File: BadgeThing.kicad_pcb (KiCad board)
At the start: 2 copper layers, 78.7 x 40.2 mm, 66 parts, among them J2 Ext 5V, J3 External 3V3, J4 SWD Header, J5 USB_C_Receptacle_USB2.0, J6 Connector_Generic_Conn_01x02, J7 Conn_01x06, SW1 ESP RESET, SW2 Left, SW3 Down, SW4 Select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

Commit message: Real final finishing touches
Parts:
- moved SW2 0.15 mm to (147.1, 128.0)
- moved SW3 0.15 mm to (154.5, 128.0)
- moved SW4 0.15 mm to (161.8, 128.0)
- moved SW5 0.15 mm to (169.2, 128.0)
- moved SW6 0.15 mm to (176.6, 128.0)
- moved D2 0.12 mm to (150.4, 97.7)
- moved D3 0.12 mm to (158.1, 97.7)
- moved D4 0.12 mm to (165.7, 97.7)
- moved D5 0.12 mm to (173.3, 97.7)
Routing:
- net GND: track 32.2 -> 34.1 mm

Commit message: consider adding an SD card slot
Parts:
- R6: value DNF -> 220 Ohm

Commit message: Actual final real finishing touches (+test pads)
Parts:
- added J10: Conn_01x01, Connector_PinHeader_2.00mm:PinHeader_1x01_P2.00mm_Vertical, B.Cu at (163.2, 111.8)
- added J11: Conn_01x01, Connector_PinHeader_2.00mm:PinHeader_1x01_P2.00mm_Vertical, B.Cu at (160.1, 100.5)
- added J12: Conn_01x01, Connector_PinHeader_2.00mm:PinHeader_1x01_P2.00mm_Vertical, B.Cu at (160.1, 102.0)
- added J8: Conn_01x01, Connector_PinHeader_2.00mm:PinHeader_1x01_P2.00mm_Vertical, B.Cu at (145.8, 119.5)
- added J9: Conn_01x01, Connector_PinHeader_2.00mm:PinHeader_1x01_P2.00mm_Vertical, B.Cu at (164.6, 111.8)
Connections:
- U3 pad 35: unconnected-(U3-GPIO23-Pad35) -> CS2
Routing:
- net +3V3: track 197.2 -> 202.2 mm
- net SCLK: track 23.9 -> 27.7 mm
- net MOSI: track 24.7 -> 28.5 mm
- net MISO: track 0.00 -> 3.66 mm
- net +5V: track 83.0 -> 86.5 mm
- net WS2812B: track 25.6 -> 27.1 mm

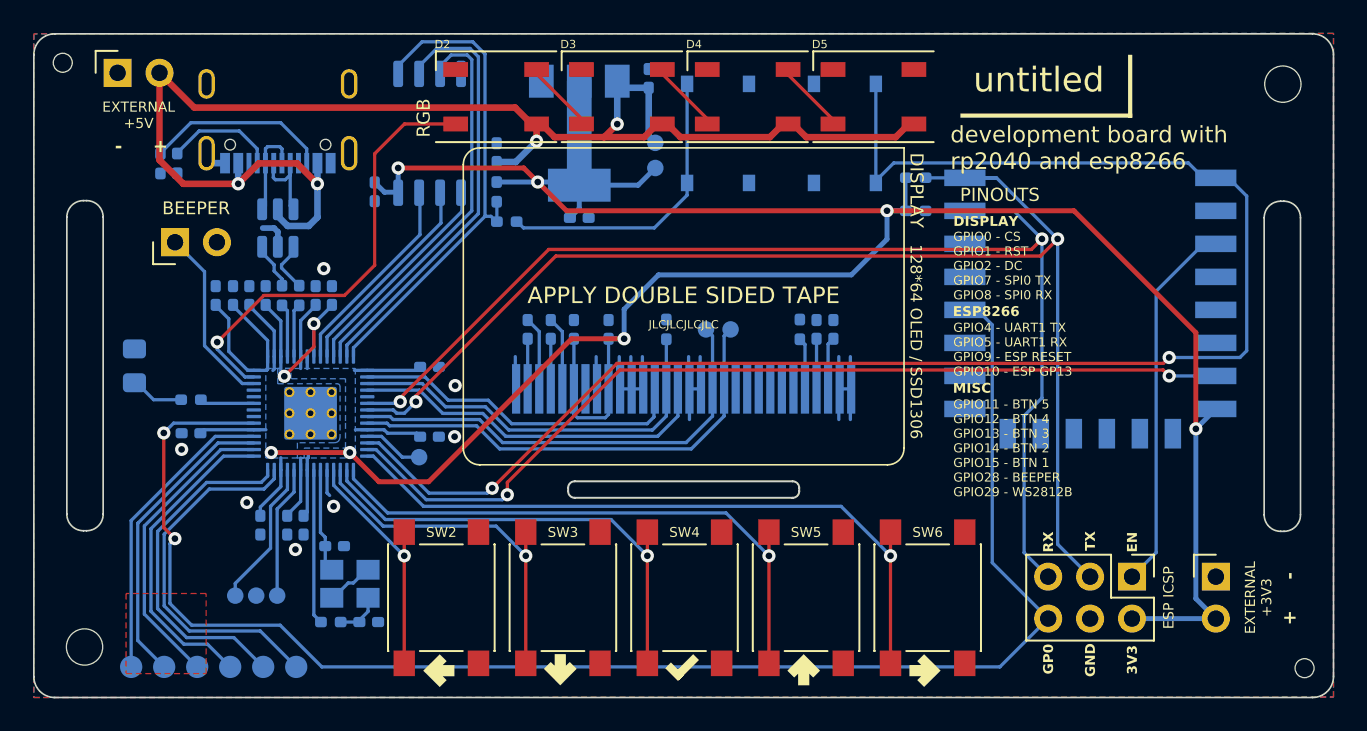
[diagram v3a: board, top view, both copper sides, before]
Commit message: Fix SPI wiring, add ESP RTS pin, add prod files
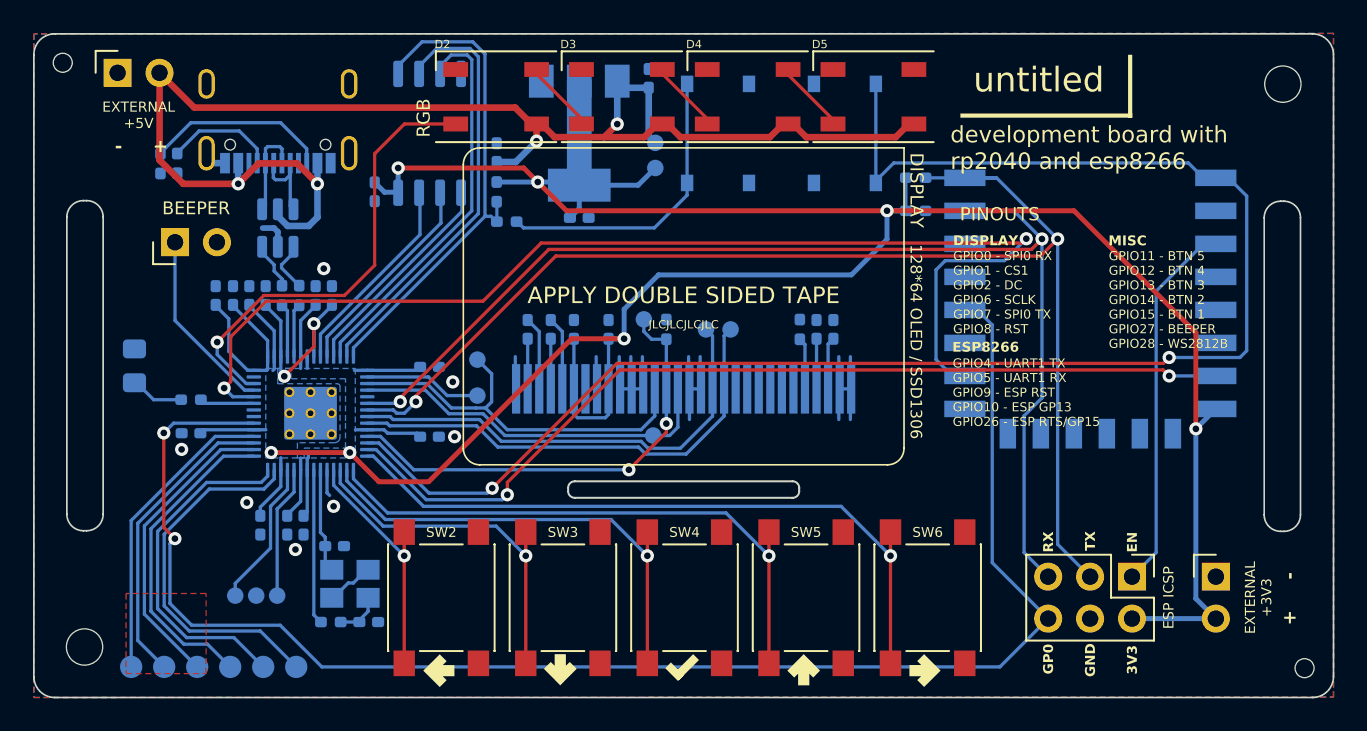
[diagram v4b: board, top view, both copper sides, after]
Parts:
- added J13: Conn_01x01, Connector_PinHeader_2.00mm:PinHeader_1x01_P2.00mm_Vertical, B.Cu at (159.4, 111.2)
- added J14: Conn_01x01, Connector_PinHeader_2.00mm:PinHeader_1x01_P2.00mm_Vertical, B.Cu at (149.3, 113.6)
- added J15: Conn_01x01, Connector_PinHeader_2.00mm:PinHeader_1x01_P2.00mm_Vertical, B.Cu at (159.9, 118.2)
- moved J8 5.14 mm to (149.3, 115.8)
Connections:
- U1 pad 16: unconnected-(U1-GPIO15-Pad16) -> ESP15
- U3 pad 11: MISO -> RST
- U3 pad 2: CS1 -> MISO
- U3 pad 3: RST -> CS1
- U3 pad 35: CS2 -> unconnected-(U3-GPIO23-Pad35)
- U3 pad 38: unconnected-(U3-GPIO26_ADC0-Pad38) -> ESP15
- U3 pad 39: unconnected-(U3-GPIO27_ADC1-Pad39) -> BEEP
- U3 pad 40: BEEP -> WS2812B
- U3 pad 41: WS2812B -> unconnected-(U3-GPIO29_ADC3-Pad41)
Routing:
- net ESP15: track 0.00 -> 69.8 mm, vias 0 -> 2
- net CS1: track 20.4 -> 24.0 mm
- net RST: track 24.2 -> 27.8 mm, vias 0 -> 2
- net MISO: track 3.66 -> 7.14 mm
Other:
- board text added: "GPIO0 - SPI0 RX GPIO1 - CS1 GPIO2 - DC GPIO6 - SCLK GPIO7 - SPI0 TX GPIO8 - RST"
- board text added: "GPIO11 - BTN 5 GPIO12 - BTN 4 GPIO13 - BTN 3 GPIO14 - BTN 2 GPIO15 - BTN 1 GPIO27 - BEEPER GPIO28 - WS2812B"
- board text added: "GPIO4 - UART1 TX GPIO5 - UART1 RX GPIO9 - ESP RST GPIO10 - ESP GP13 GPIO26 - ESP RTS/GP15"
- board text removed: "GPIO0 - CS GPIO1 - RST GPIO2 - DC GPIO7 - SPI0 TX GPIO8 - SPI0 RX"
- board text removed: "GPIO11 - BTN 5 GPIO12 - BTN 4 GPIO13 - BTN 3 GPIO14 - BTN 2 GPIO15 - BTN 1 GPIO28 - BEEPER GPIO29 - WS2812B"
- board text removed: "GPIO4 - UART1 TX GPIO5 - UART1 RX GPIO9 - ESP RESET GPIO10 - ESP GP13"
